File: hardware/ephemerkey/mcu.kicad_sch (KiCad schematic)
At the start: 22 parts, among them J1 SWD TC2030-NL, J2 LOCK OUT, SW1 USER1, SW2 USER2, SW3 USER3/DFU, U1 STM32U083KCU6, Y1 32.768kHz

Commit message: MCU 3D model: use KiCad's generic QFN-32 model for the UFQFPN-32
KiCad ships no model for the ultra-thin UFQFPN-32, but it does ship a generic
QFN-32-1EP_5x5mm_P0.5mm_EP3.45x3.45mm (same 5x5 body, 0.5mm pitch, exposed pad —
only the body height differs). Vendored a project copy of the UFQFPN-32
footprint (ephemerkey:UFQFPN-32-1EP_5x5mm_P0.5mm_EP3.5x3.5mm) with its (model)
repointed to that generic QFN model. No STEP file needed (model is in KiCad's
3D dir). So the MCU now renders; only W3011A still needs a downloaded model.

DESIGN.md library map + 3D note, PARTS.md, 3dmodels README updated. make check:
60 components, 60/60 footprints, no dup refs.

Co-Authored-By: Claude Opus 4.8 (1M context) <noreply@anthropic.com>
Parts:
- U1: footprint Package_DFN_QFN:UFQFPN-32-1EP_5x5mm_P0.5mm_EP3.5x3.5mm -> ephemerkey:UFQFPN-32-1EP_5x5mm_P0.5mm_EP3.5x3.5mm
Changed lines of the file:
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@@
 			(effects (font (size 1.27 1.27)) (justify left))
 		)
-		(property "Footprint" "Package_DFN_QFN:UFQFPN-32-1EP_5x5mm_P0.5mm_EP3.5x3.5mm"
+		(property "Footprint" "ephemerkey:UFQFPN-32-1EP_5x5mm_P0.5mm_EP3.5x3.5mm"
 			(at 45.7200 55.8800 0)
 			(effects (font (size 1.27 1.27))) (hide yes)
@@
 		(instances
 			(project "ephemerkey"
-				(path "/e1000000-0000-4000-8000-000000000001/8f68bf2c-35b7-40f9-b8ab-785f56914c2e"
+				(path "/e1000000-0000-4000-8000-000000000001/686b0f92-d7cc-4084-9010-1c5dad5f43f0"
 					(reference "U1")
 					(unit 1)
@@
 		(instances
 			(project "ephemerkey"
-				(path "/e1000000-0000-4000-8000-000000000001/8f68bf2c-35b7-40f9-b8ab-785f56914c2e"
+				(path "/e1000000-0000-4000-8000-000000000001/686b0f92-d7cc-4084-9010-1c5dad5f43f0"
 					(reference "J1")
 					(unit 1)
@@
 		(instances
 			(project "ephemerkey"
-				(path "/e1000000-0000-4000-8000-000000000001/8f68bf2c-35b7-40f9-b8ab-785f56914c2e"
+				(path "/e1000000-0000-4000-8000-000000000001/686b0f92-d7cc-4084-9010-1c5dad5f43f0"
 					(reference "J2")
 					(unit 1)
@@
 		(instances
 			(project "ephemerkey"
-				(path "/e1000000-0000-4000-8000-000000000001/8f68bf2c-35b7-40f9-b8ab-785f56914c2e"
+				(path "/e1000000-0000-4000-8000-000000000001/686b0f92-d7cc-4084-9010-1c5dad5f43f0"
 					(reference "DS1")
 					(unit 1)
@@
 		(instances
 			(project "ephemerkey"
-				(path "/e1000000-0000-4000-8000-000000000001/8f68bf2c-35b7-40f9-b8ab-785f56914c2e"
+				(path "/e1000000-0000-4000-8000-000000000001/686b0f92-d7cc-4084-9010-1c5dad5f43f0"
 					(reference "Y1")
 					(unit 1)
@@
 		(instances
 			(project "ephemerkey"
-				(path "/e1000000-0000-4000-8000-000000000001/8f68bf2c-35b7-40f9-b8ab-785f56914c2e"
+				(path "/e1000000-0000-4000-8000-000000000001/686b0f92-d7cc-4084-9010-1c5dad5f43f0"
 					(reference "C1")
 					(unit 1)
@@
 		(instances
 			(project "ephemerkey"
-				(path "/e1000000-0000-4000-8000-000000000001/8f68bf2c-35b7-40f9-b8ab-785f56914c2e"
+				(path "/e1000000-0000-4000-8000-000000000001/686b0f92-d7cc-4084-9010-1c5dad5f43f0"
 					(reference "C2")
 					(unit 1)
@@
 		(instances
 			(project "ephemerkey"
-				(path "/e1000000-0000-4000-8000-000000000001/8f68bf2c-35b7-40f9-b8ab-785f56914c2e"
+				(path "/e1000000-0000-4000-8000-000000000001/686b0f92-d7cc-4084-9010-1c5dad5f43f0"
 					(reference "C3")
 					(unit 1)
@@
 		(instances
 			(project "ephemerkey"
-				(path "/e1000000-0000-4000-8000-000000000001/8f68bf2c-35b7-40f9-b8ab-785f56914c2e"
+				(path "/e1000000-0000-4000-8000-000000000001/686b0f92-d7cc-4084-9010-1c5dad5f43f0"
 					(reference "C4")
 					(unit 1)
@@
 		(instances
 			(project "ephemerkey"
-				(path "/e1000000-0000-4000-8000-000000000001/8f68bf2c-35b7-40f9-b8ab-785f56914c2e"
+				(path "/e1000000-0000-4000-8000-000000000001/686b0f92-d7cc-4084-9010-1c5dad5f43f0"
 					(reference "C5")
 					(unit 1)
@@
 		(instances
 			(project "ephemerkey"
-				(path "/e1000000-0000-4000-8000-000000000001/8f68bf2c-35b7-40f9-b8ab-785f56914c2e"
+				(path "/e1000000-0000-4000-8000-000000000001/686b0f92-d7cc-4084-9010-1c5dad5f43f0"
 					(reference "C6")
 					(unit 1)
@@
 		(instances
 			(project "ephemerkey"
-				(path "/e1000000-0000-4000-8000-000000000001/8f68bf2c-35b7-40f9-b8ab-785f56914c2e"
+				(path "/e1000000-0000-4000-8000-000000000001/686b0f92-d7cc-4084-9010-1c5dad5f43f0"
 					(reference "C7")
 					(unit 1)
@@
 		(instances
 			(project "ephemerkey"
-				(path "/e1000000-0000-4000-8000-000000000001/8f68bf2c-35b7-40f9-b8ab-785f56914c2e"
+				(path "/e1000000-0000-4000-8000-000000000001/686b0f92-d7cc-4084-9010-1c5dad5f43f0"
 					(reference "C8")
 					(unit 1)
@@
 		(instances
 			(project "ephemerkey"
-				(path "/e1000000-0000-4000-8000-000000000001/8f68bf2c-35b7-40f9-b8ab-785f56914c2e"
+				(path "/e1000000-0000-4000-8000-000000000001/686b0f92-d7cc-4084-9010-1c5dad5f43f0"
 					(reference "C9")
 					(unit 1)
@@
 		(instances
 			(project "ephemerkey"
-				(path "/e1000000-0000-4000-8000-000000000001/8f68bf2c-35b7-40f9-b8ab-785f56914c2e"
+				(path "/e1000000-0000-4000-8000-000000000001/686b0f92-d7cc-4084-9010-1c5dad5f43f0"
 					(reference "R1")
 					(unit 1)
@@
 		(instances
 			(project "ephemerkey"
-				(path "/e1000000-0000-4000-8000-000000000001/8f68bf2c-35b7-40f9-b8ab-785f56914c2e"
+				(path "/e1000000-0000-4000-8000-000000000001/686b0f92-d7cc-4084-9010-1c5dad5f43f0"
 					(reference "SW1")
 					(unit 1)
@@
 		(instances
 			(project "ephemerkey"
-				(path "/e1000000-0000-4000-8000-000000000001/8f68bf2c-35b7-40f9-b8ab-785f56914c2e"
+				(path "/e1000000-0000-4000-8000-000000000001/686b0f92-d7cc-4084-9010-1c5dad5f43f0"
 					(reference "SW2")
 					(unit 1)
@@
 		(instances
 			(project "ephemerkey"
-				(path "/e1000000-0000-4000-8000-000000000001/8f68bf2c-35b7-40f9-b8ab-785f56914c2e"
+				(path "/e1000000-0000-4000-8000-000000000001/686b0f92-d7cc-4084-9010-1c5dad5f43f0"
 					(reference "SW3")
 					(unit 1)
@@
 		(instances
 			(project "ephemerkey"
-				(path "/e1000000-0000-4000-8000-000000000001/8f68bf2c-35b7-40f9-b8ab-785f56914c2e"
+				(path "/e1000000-0000-4000-8000-000000000001/686b0f92-d7cc-4084-9010-1c5dad5f43f0"
 					(reference "D1")
 					(unit 1)
@@
 		(instances
 			(project "ephemerkey"
-				(path "/e1000000-0000-4000-8000-000000000001/8f68bf2c-35b7-40f9-b8ab-785f56914c2e"
+				(path "/e1000000-0000-4000-8000-000000000001/686b0f92-d7cc-4084-9010-1c5dad5f43f0"
 					(reference "R2")
 					(unit 1)
@@
 		(instances
 			(project "ephemerkey"
-				(path "/e1000000-0000-4000-8000-000000000001/8f68bf2c-35b7-40f9-b8ab-785f56914c2e"
+				(path "/e1000000-0000-4000-8000-000000000001/686b0f92-d7cc-4084-9010-1c5dad5f43f0"
 					(reference "D2")
 					(unit 1)
@@
 		(instances
 			(project "ephemerkey"
-				(path "/e1000000-0000-4000-8000-000000000001/8f68bf2c-35b7-40f9-b8ab-785f56914c2e"
+				(path "/e1000000-0000-4000-8000-000000000001/686b0f92-d7cc-4084-9010-1c5dad5f43f0"
 					(reference "R3")
 					(unit 1)

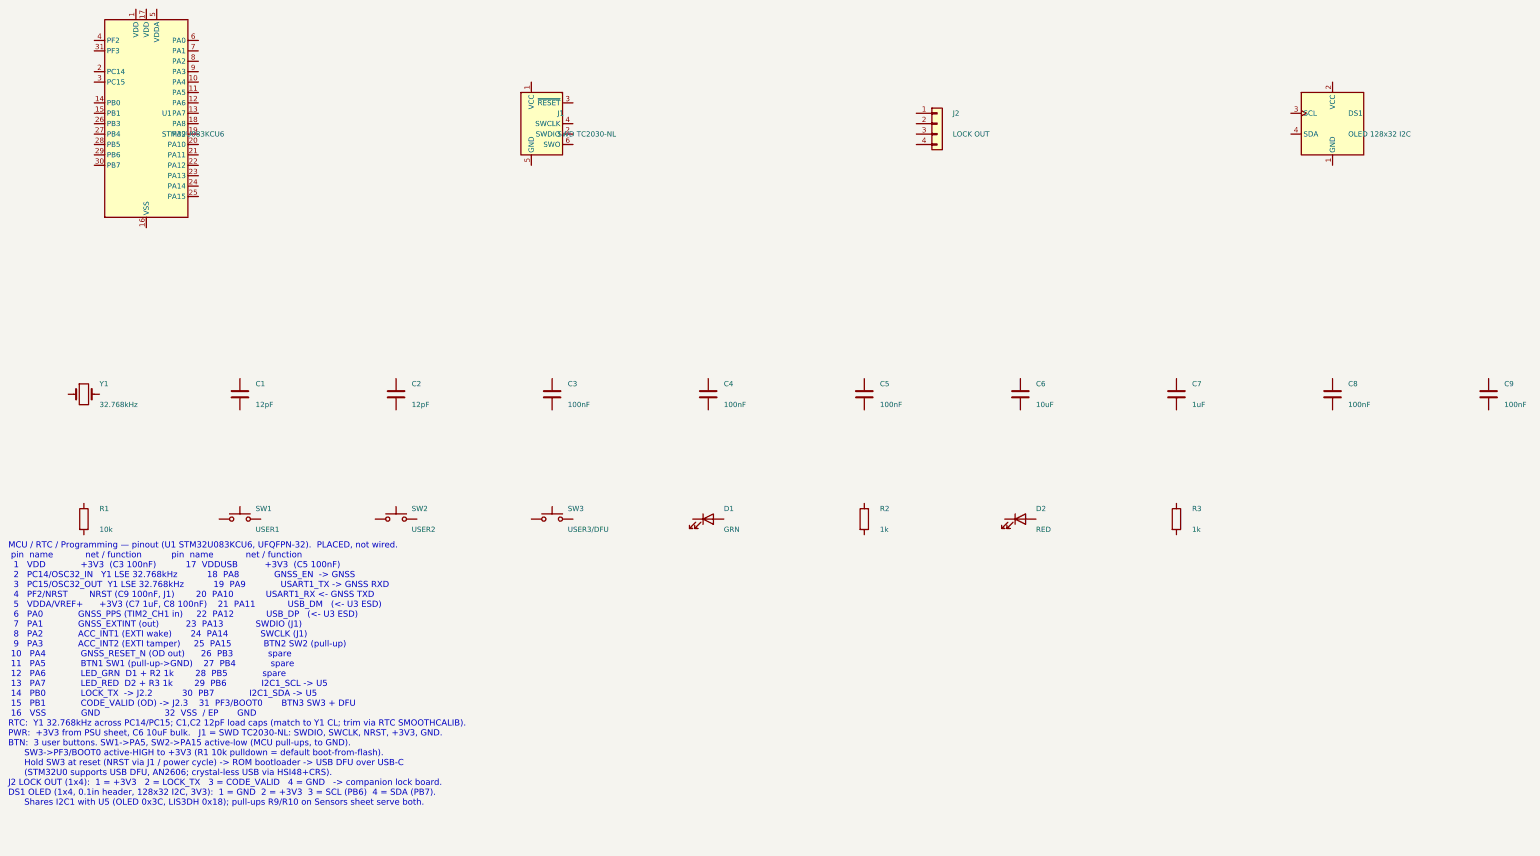
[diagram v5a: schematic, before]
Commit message: lock: add companion TOTP lock board + authenticated lock interface
Add hardware/lock — a second PCB in this repo (shares scripts/kschgen.py,
Makefile, and lib tables, like reefvolt-sensorbuddy):
- ATtiny1616 controller running directly off the 1S cell (no LDO, ~0.1uA
  power-down), a gated MT3608 boost to 12V with a reservoir cap, and an
  AO3400A + SS34 low-side peak-and-hold solenoid driver. All-JLCPCB BOM.
- Authenticated digital link to ephemerkey: 4-wire UART + firmware
  HMAC-SHA1 challenge-response (reuses smalltotp; nonce anti-replay;
  pairing secret in flash). UPDI programming header (J4).
- Sheets are placed-not-wired; on-canvas notes carry the wiring spec.

ephemerkey side:
- Rework J2 from the one-way LOCK_OUT strobe to the matching authenticated
  UART (KEY_TX/KEY_RX + CODE_REQ wake on PB3).
- DESIGN.md: authenticated interface contract + firmware plan; pin table.
- Regenerate sheets (manifest-driven; regen reassigns UUIDs).

hardware/Makefile: add `lock` to PROJECTS.

Co-Authored-By: Claude Opus 4.8 (1M context) <noreply@anthropic.com>
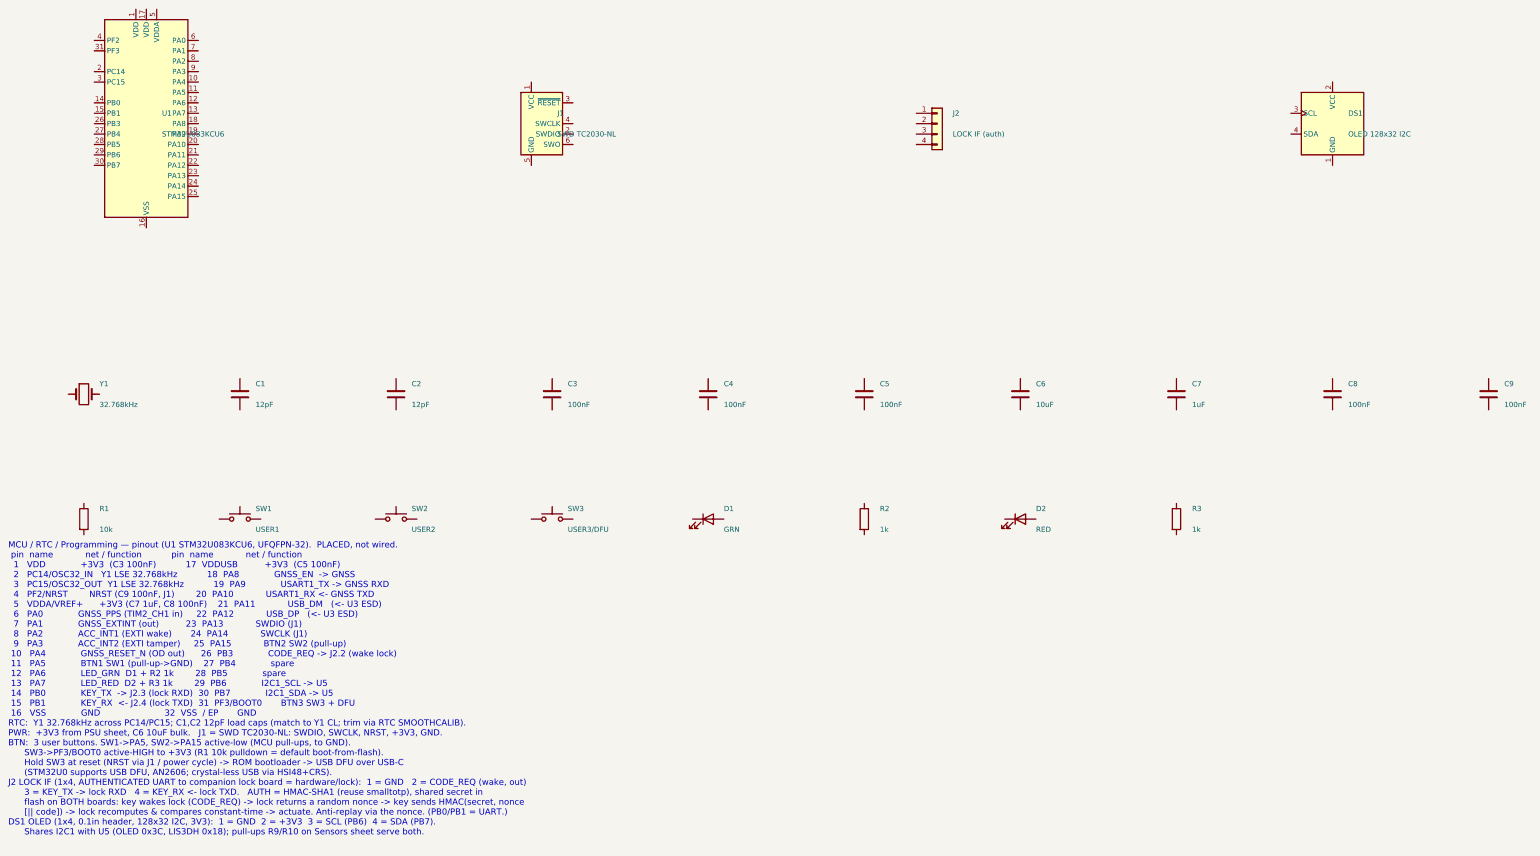
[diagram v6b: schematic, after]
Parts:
- J2: value LOCK OUT -> LOCK IF (auth)

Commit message: lock: switch ephemerkey<->lock link to master-driven I2C (wake-on-I2C)
Replace the 4-wire authenticated UART with a 3-wire authenticated I2C bus:
- ephemerkey is the I2C master, the lock (ATtiny1616) is the target (0x60).
  Challenge-response is master-driven: read the nonce, then write the
  HMAC-SHA1(secret, nonce||code).
- Drop the discrete CODE_REQ wake line (don't mix a button-style input with
  the bus). The lock wakes from power-down on the first I2C START (pin-change
  interrupt on SCL); the master sends a dummy/wake xfer then retries.
- 3-wire J2 (GND/SCL/SDA), 1x3 on both boards.
- I2C pull-ups R11/R12 (4.7k) on ephemerkey's 3V3 (master side) -- the lock
  runs at VBAT, so master-side pull-ups avoid the 3V3/VBAT cross-domain.

ephemerkey: PB0=SDA, PB1=SCL, PB3 freed to spare; add R11/R12; regenerate.
lock: PB0=SCL+wake, PB1=SDA, PA4 freed; J2 -> 1x3; regenerate.
Docs (DESIGN.md, hardware/lock/README.md) updated to match.

Co-Authored-By: Claude Opus 4.8 (1M context) <noreply@anthropic.com>
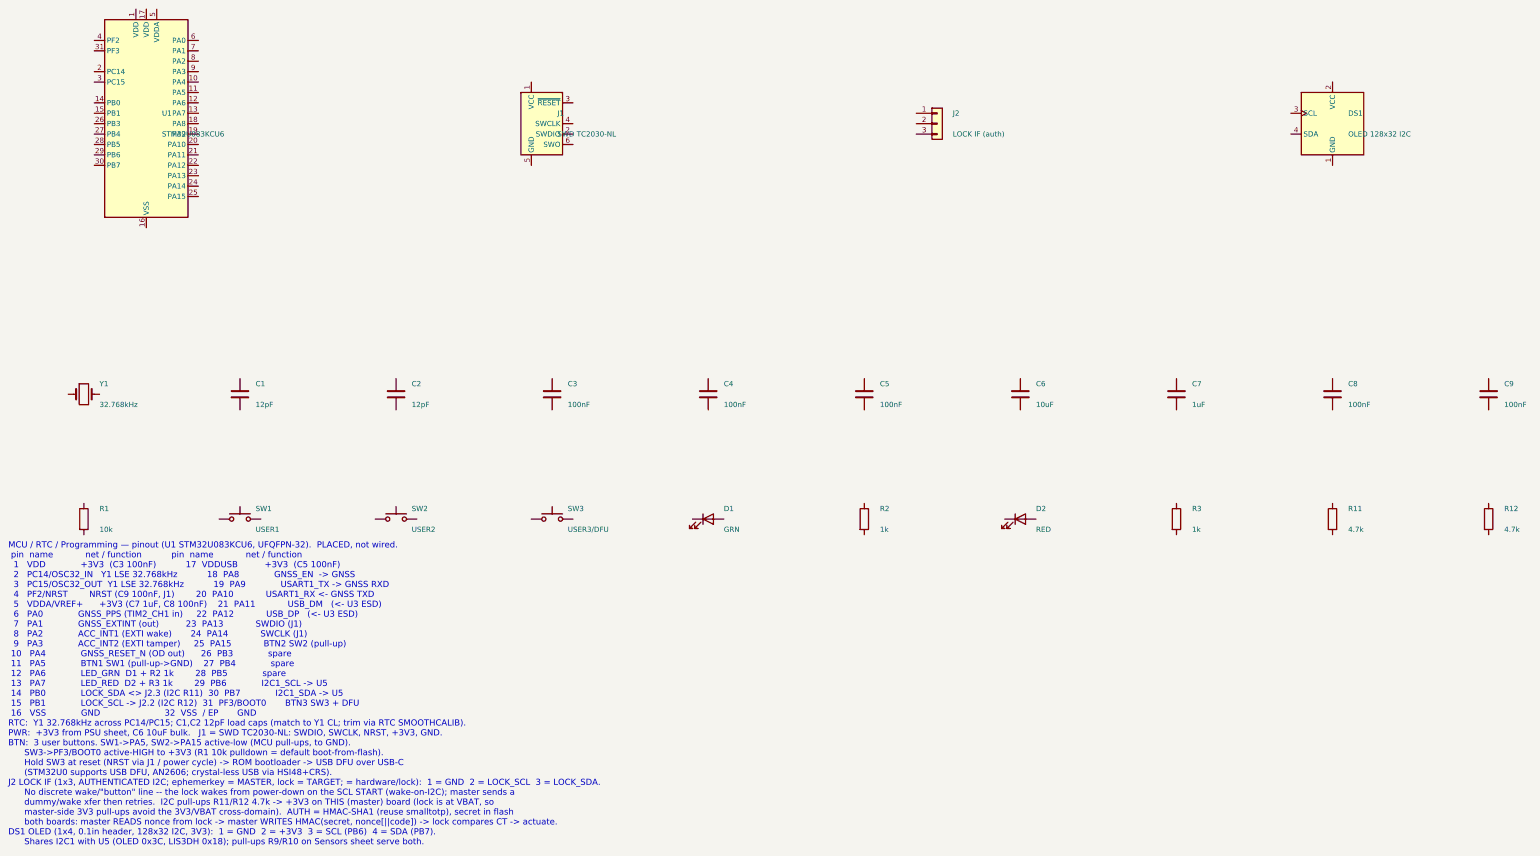
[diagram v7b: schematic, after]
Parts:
- removed J2: LOCK IF (auth), Connector_PinHeader_2.54mm:PinHeader_1x04_P2.54mm_Vertical, symbol Connector_Generic:Conn_01x04
- added J2: LOCK IF (auth), Connector_PinHeader_2.54mm:PinHeader_1x03_P2.54mm_Vertical, symbol Connector_Generic:Conn_01x03
- added R11, R12: 4.7k, Resistor_SMD:R_0402_1005Metric, symbol Device:R

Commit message: lock: servo option, firmware boost/power control, hall sensors, I2C protocol
Checkpoint of the companion lock board evolution:
- I2C link connector -> right-angle 4-pin JST-PH (S4B-PH-K, C157926);
  VCC is No-Connect on the lock (don't bridge the two battery rails).
- Add a parallel servo actuator option (J5) beside the 12V solenoid; one
  fully-populated board can carry both, one active at a time.
- Firmware-selectable boost: BOOST_VSEL (Q2 + R17 switch the FB divider)
  -> 6V (servo, default) or 12V (solenoid).  R4 22k / R17 20k.
- Servo high-side load switch (Q3 P-FET + Q4 driver, SERVO_PWR_EN) with a
  hardware interlock (Q5) that forces servo power OFF whenever boost = 12V,
  so a 12V solenoid pulse can never reach a 6V servo.
- Door/bolt hall sensors (J6/J7, S3B-PH-K) powered from a GPIO (HALL_PWR)
  so they draw ~0uA when the lock sleeps.
- I2C register/command protocol: STATUS (door/bolt/actuator probe, no auth),
  NONCE (read), COMMAND (authenticated UNLOCK/LOCK; LOCK drives a servo to the
  lock angle).  HMAC-SHA1 challenge-response, reuses smalltotp.

All footprints are KiCad-bundled (every part carries a 3D model). Board
regenerates + checks clean (46 components). Docs: hardware/lock/README.md and
DESIGN.md updated.

Co-Authored-By: Claude Opus 4.8 (1M context) <noreply@anthropic.com>
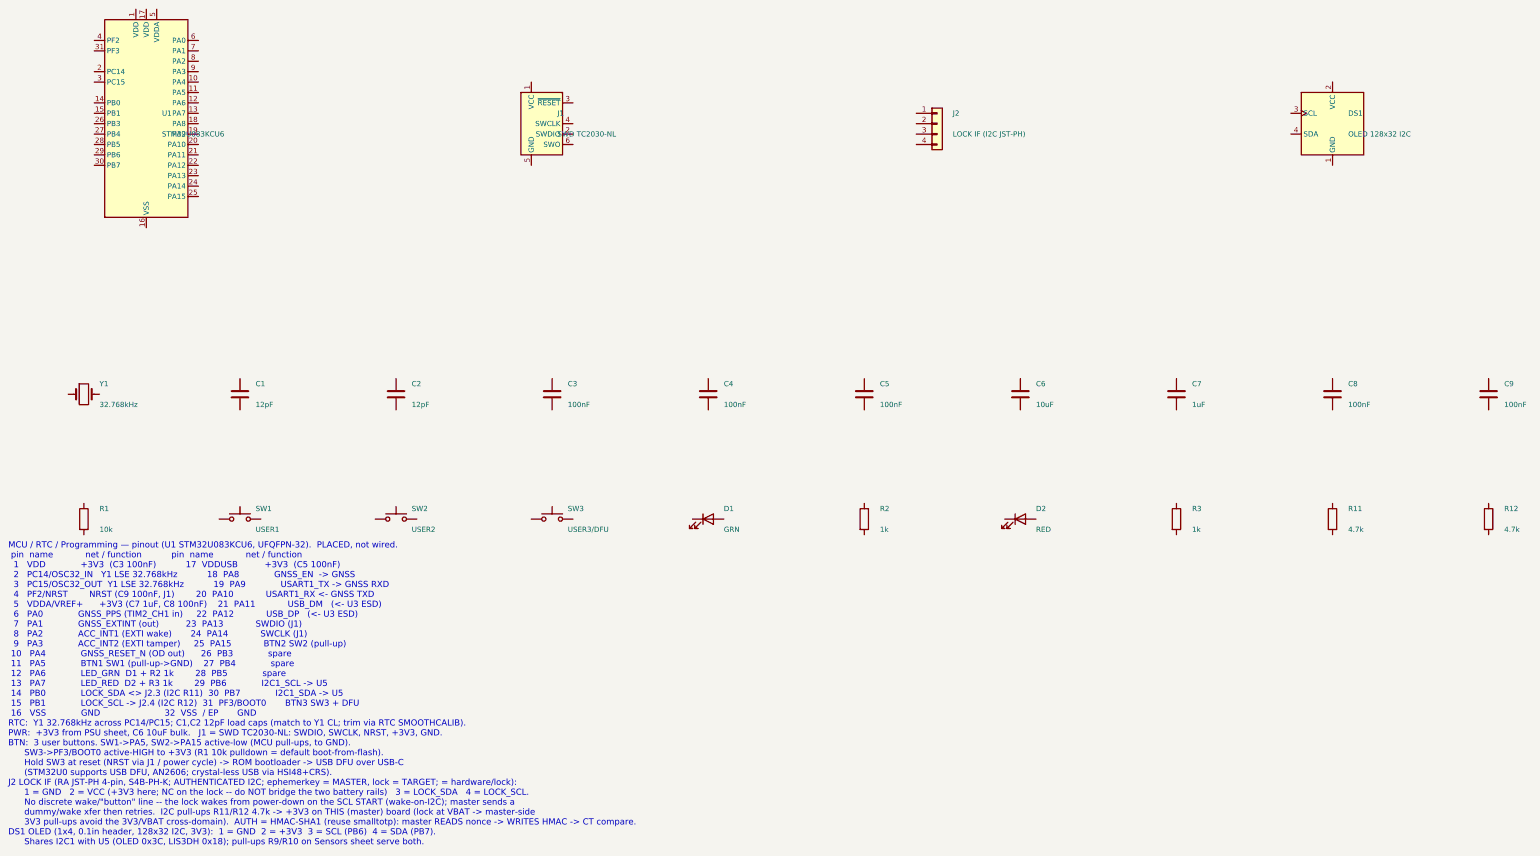
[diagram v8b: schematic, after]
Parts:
- removed J2: LOCK IF (auth), Connector_PinHeader_2.54mm:PinHeader_1x03_P2.54mm_Vertical, symbol Connector_Generic:Conn_01x03
- added J2: LOCK IF (I2C JST-PH), Connector_JST:JST_PH_S4B-PH-K_1x04_P2.00mm_Horizontal, symbol Connector_Generic:Conn_01x04
